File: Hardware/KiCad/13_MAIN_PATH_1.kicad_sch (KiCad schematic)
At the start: 0 parts

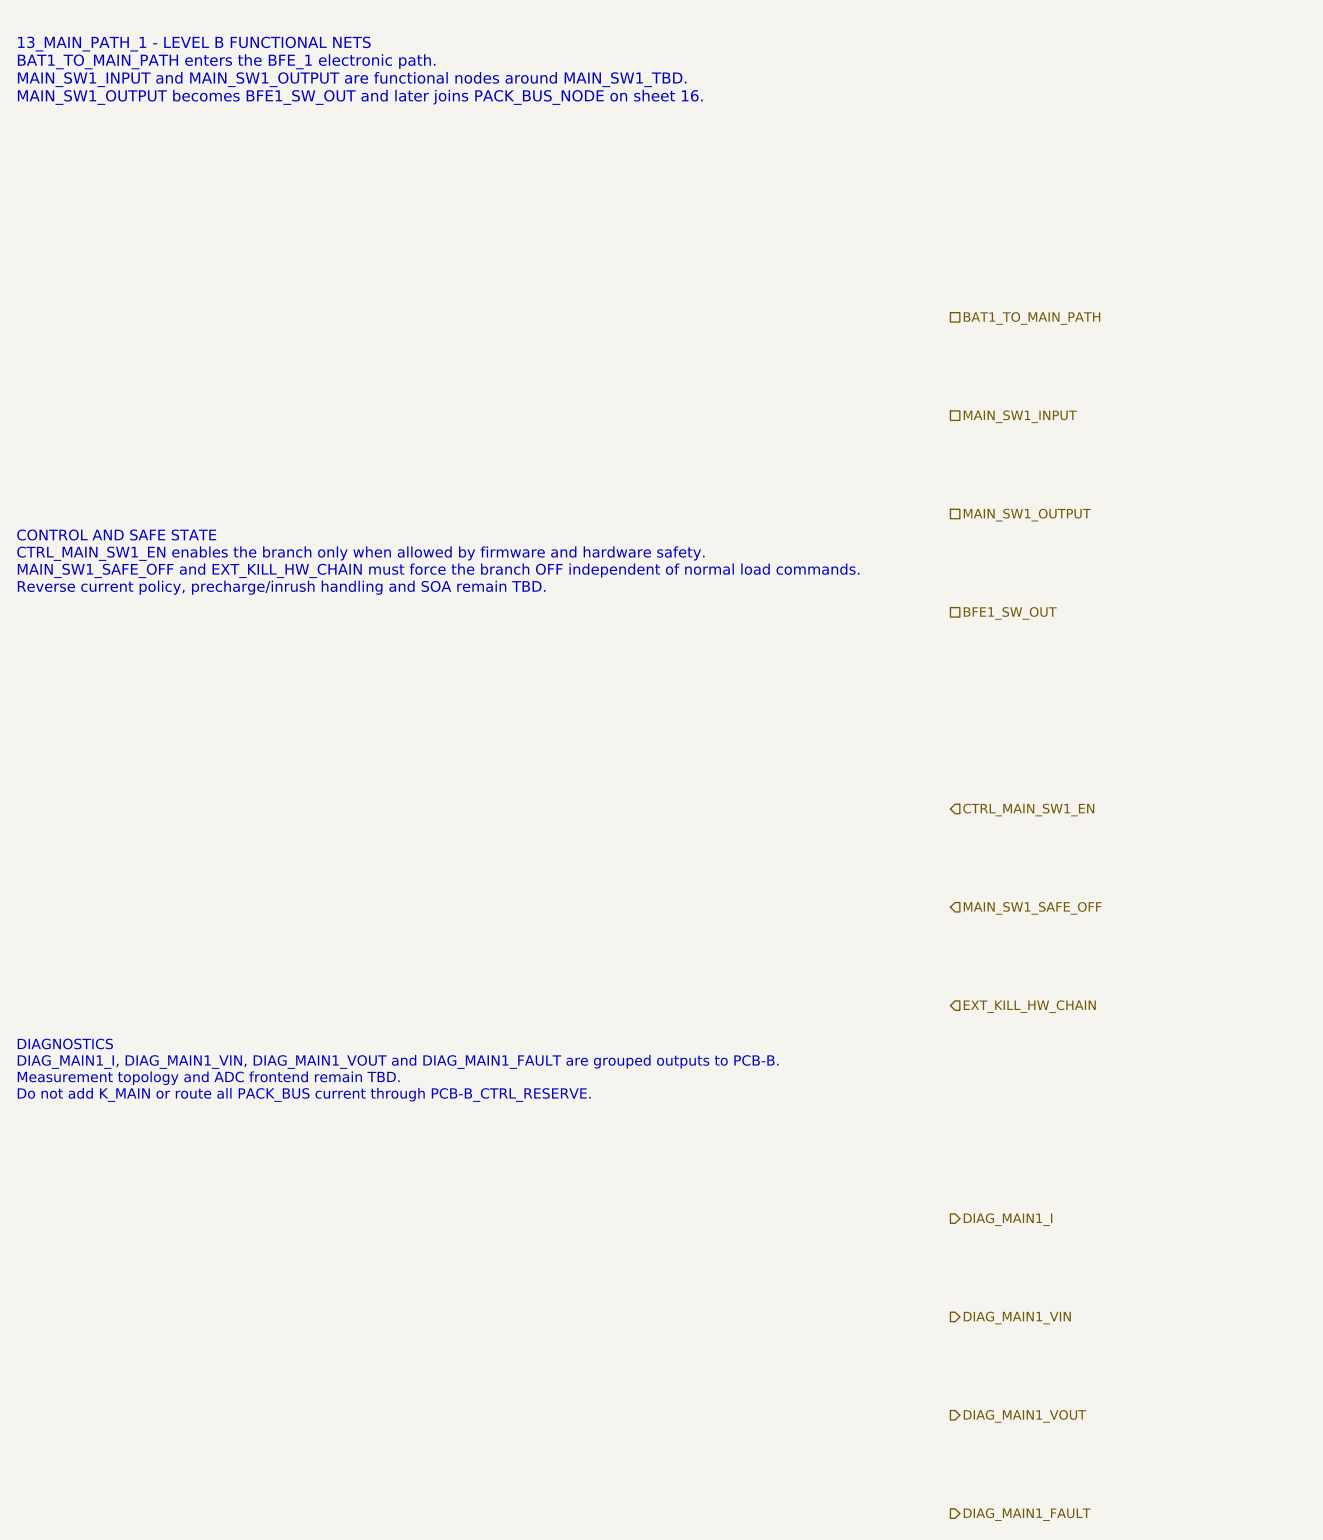
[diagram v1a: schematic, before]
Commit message: hardware: add MAIN_SW1 symbol skeleton zones
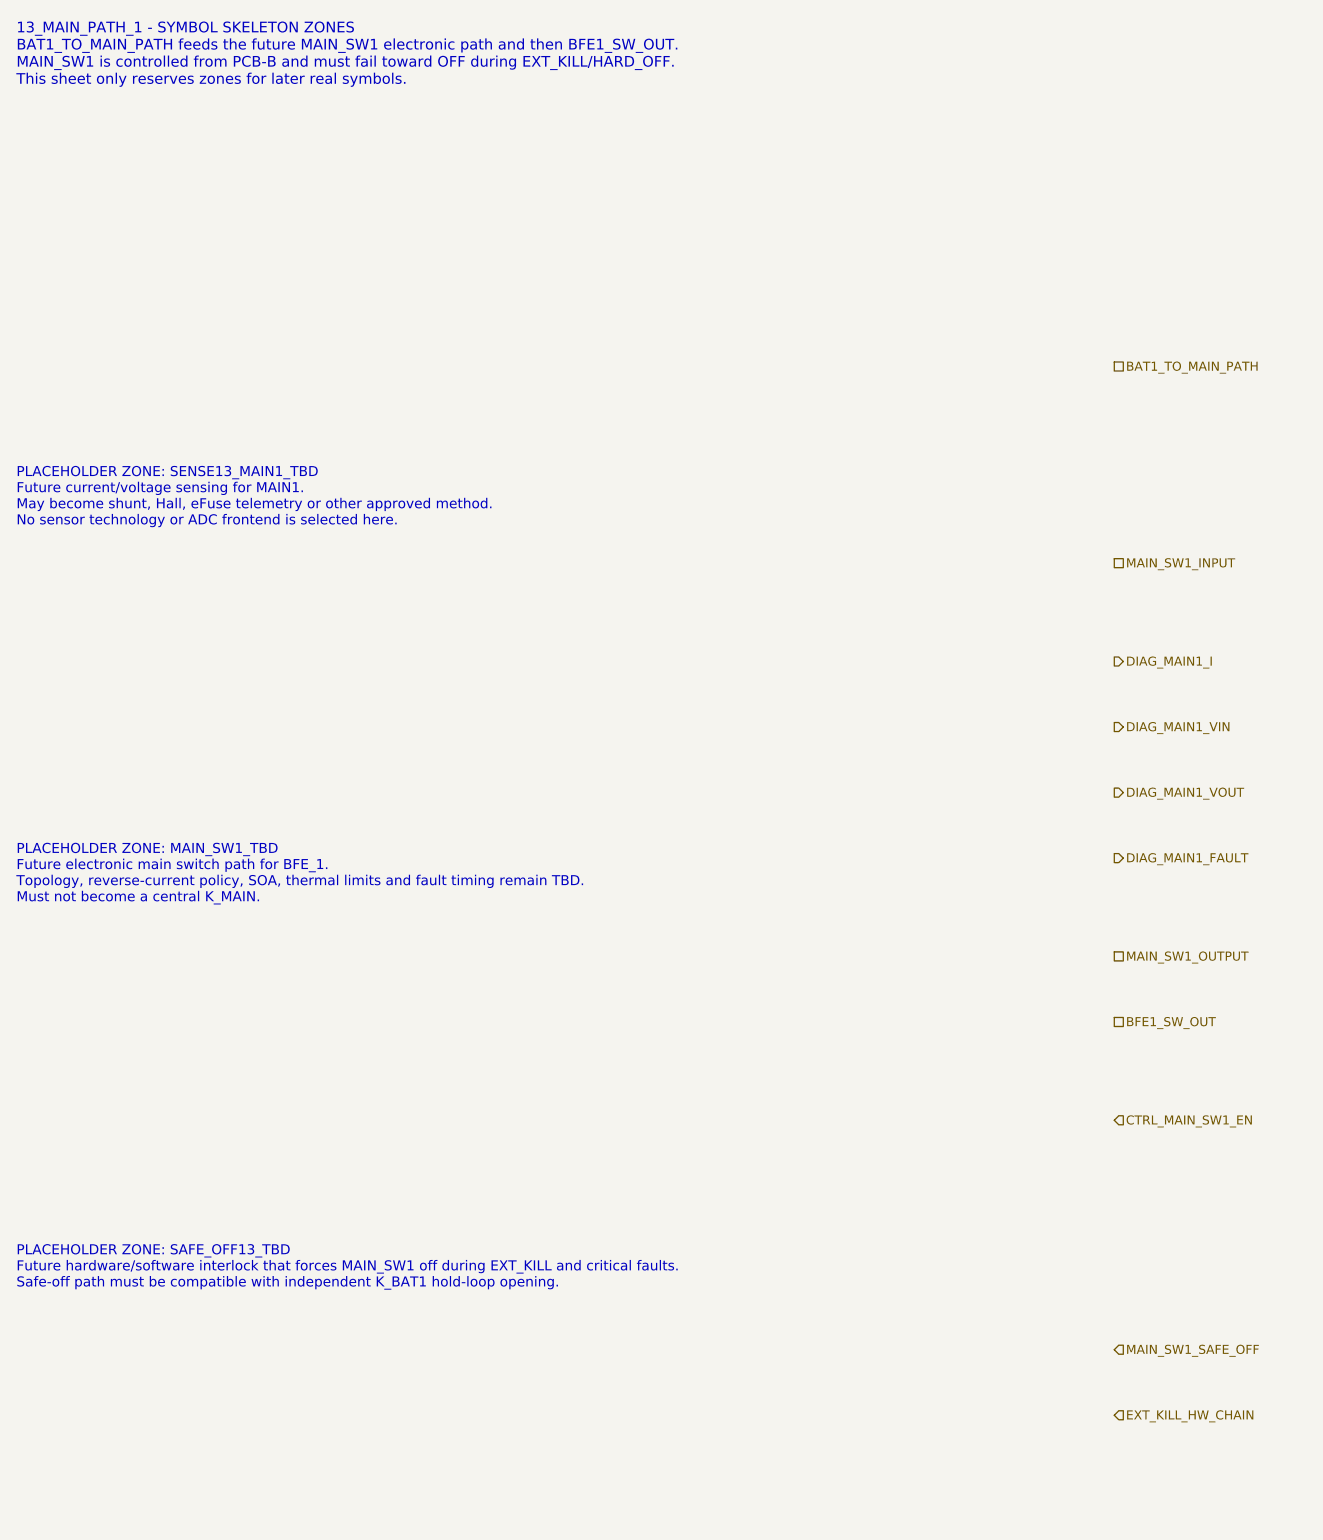
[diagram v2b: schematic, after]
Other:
- note added: "13_MAIN_PATH_1 - SYMBOL SKELETON ZONES BAT1_TO_MAIN_PATH feeds the future MAIN_SW1 electronic path and then BFE1_SW_OUT. MAIN_SW1 is controlled from PCB-B and must fail toward OFF during EXT_KILL/HARD_OFF. This sheet only reserves zones for later real symbols."
- note added: "PLACEHOLDER ZONE: MAIN_SW1_TBD Future electronic main switch path for BFE_1. Topology, reverse-current policy, SOA, thermal limits and fault timing remain TBD. Must not become a central K_MAIN."
- note added: "PLACEHOLDER ZONE: SAFE_OFF13_TBD Future hardware/software interlock that forces MAIN_SW1 off during EXT_KILL and critical faults. Safe-off path must be compatible with independent K_BAT1 hold-loop opening."
- note added: "PLACEHOLDER ZONE: SENSE13_MAIN1_TBD Future current/voltage sensing for MAIN1. May become shunt, Hall, eFuse telemetry or other approved method. No sensor technology or ADC frontend is selected here."
- note removed: "13_MAIN_PATH_1 - LEVEL B FUNCTIONAL NETS BAT1_TO_MAIN_PATH enters the BFE_1 electronic path. MAIN_SW1_INPUT and MAIN_SW1_OUTPUT are functional nodes around MAIN_SW1_TBD. MAIN_SW1_OUTPUT becomes BFE1_SW_OUT and later joins PACK_BUS_NODE on sheet 16."
- note removed: "CONTROL AND SAFE STATE CTRL_MAIN_SW1_EN enables the branch only when allowed by firmware and hardware safety. MAIN_SW1_SAFE_OFF and EXT_KILL_HW_CHAIN must force the branch OFF independent of normal load commands. Reverse current policy, precharge/inrush handling and SOA remain TBD."
- note removed: "DIAGNOSTICS DIAG_MAIN1_I, DIAG_MAIN1_VIN, DIAG_MAIN1_VOUT and DIAG_MAIN1_FAULT are grouped outputs to PCB-B. Measurement topology and ADC frontend remain TBD. Do not add K_MAIN or route all PACK_BUS current through PCB-B_CTRL_RESERVE."
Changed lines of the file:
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@@
 		(title "13_MAIN_PATH_1 - BFE_1 main electronic path")
 		(date "2026-07-15")
-		(rev "B1")
+		(rev "C1")
 		(company "Gonoboben/plataVM")
-		(comment 1 "Architecture Level B: MAIN_SW1 control, diagnostics and safe-state nets")
-		(comment 2 "No MAIN_SW1 topology, MOSFET, eFuse or current sensor selected")
+		(comment 1 "Symbol skeleton: MAIN_SW1, sensing and safe-off placeholders")
+		(comment 2 "No MOSFET, eFuse, ideal-diode, current sensor or footprint selected")
 	)
-	(text "13_MAIN_PATH_1 - LEVEL B FUNCTIONAL NETS\nBAT1_TO_MAIN_PATH enters the BFE_1 electronic path.\nMAIN_SW1_INPUT and MAIN_SW1_OUTPUT are functional nodes around MAIN_SW1_TBD.\nMAIN_SW1_OUTPUT becomes BFE1_SW_OUT and later joins PACK_BUS_NODE on sheet 16."
+	(text "13_MAIN_PATH_1 - SYMBOL SKELETON ZONES\nBAT1_TO_MAIN_PATH feeds the future MAIN_SW1 electronic path and then BFE1_SW_OUT.\nMAIN_SW1 is controlled from PCB-B and must fail toward OFF during EXT_KILL/HARD_OFF.\nThis sheet only reserves zones for later real symbols."
 		(exclude_from_sim no)
-		(at 12 18 0)
-		(effects (font (size 1.35 1.35)) (justify left))
+		(at 12 16 0)
+		(effects (font (size 1.3 1.3)) (justify left))
 		(uuid "bfe-lb-00000013-0000-4000-8000-000000000101")
 	)
-	(text "CONTROL AND SAFE STATE\nCTRL_MAIN_SW1_EN enables the branch only when allowed by firmware and hardware safety.\nMAIN_SW1_SAFE_OFF and EXT_KILL_HW_CHAIN must force the branch OFF independent of normal load commands.\nReverse current policy, precharge/inrush handling and SOA remain TBD."
+	(text "PLACEHOLDER ZONE: SENSE13_MAIN1_TBD\nFuture current/voltage sensing for MAIN1.\nMay become shunt, Hall, eFuse telemetry or other approved method.\nNo sensor technology or ADC frontend is selected here."
 		(exclude_from_sim no)
-		(at 12 78 0)
-		(effects (font (size 1.3 1.3)) (justify left))
+		(at 12 70 0)
+		(effects (font (size 1.22 1.22)) (justify left))
 		(uuid "bfe-lb-00000013-0000-4000-8000-000000000102")
 	)
-	(text "DIAGNOSTICS\nDIAG_MAIN1_I, DIAG_MAIN1_VIN, DIAG_MAIN1_VOUT and DIAG_MAIN1_FAULT are grouped outputs to PCB-B.\nMeasurement topology and ADC frontend remain TBD.\nDo not add K_MAIN or route all PACK_BUS current through PCB-B_CTRL_RESERVE."
+	(text "PLACEHOLDER ZONE: MAIN_SW1_TBD\nFuture electronic main switch path for BFE_1.\nTopology, reverse-current policy, SOA, thermal limits and fault timing remain TBD.\nMust not become a central K_MAIN."
 		(exclude_from_sim no)
-		(at 12 140 0)
-		(effects (font (size 1.25 1.25)) (justify left))
+		(at 12 116 0)
+		(effects (font (size 1.22 1.22)) (justify left))
 		(uuid "bfe-lb-00000013-0000-4000-8000-000000000103")
 	)
-	(hierarchical_label "BAT1_TO_MAIN_PATH" (shape passive) (exclude_from_sim no) (at 126 48 0) (effects (font (size 1.15 1.15)) (justify left)) (uuid "bfe-lb-00000013-0000-4000-8000-000000000201"))
-	(hierarchical_label "MAIN_SW1_INPUT" (shape passive) (exclude_from_sim no) (at 126 60 0) (effects (font (size 1.15 1.15)) (justify left)) (uuid "bfe-lb-00000013-0000-4000-8000-000000000202"))
-	(hierarchical_label "MAIN_SW1_OUTPUT" (shape passive) (exclude_from_sim no) (at 126 72 0) (effects (font (size 1.15 1.15)) (justify left)) (uuid "bfe-lb-00000013-0000-4000-8000-000000000203"))
-	(hierarchical_label "BFE1_SW_OUT" (shape passive) (exclude_from_sim no) (at 126 84 0) (effects (font (size 1.15 1.15)) (justify left)) (uuid "bfe-lb-00000013-0000-4000-8000-000000000204"))
-	(hierarchical_label "CTRL_MAIN_SW1_EN" (shape input) (exclude_from_sim no) (at 126 108 0) (effects (font (size 1.15 1.15)) (justify left)) (uuid "bfe-lb-00000013-0000-4000-8000-000000000205"))
-	(hierarchical_label "MAIN_SW1_SAFE_OFF" (shape input) (exclude_from_sim no) (at 126 120 0) (effects (font (size 1.15 1.15)) (justify left)) (uuid "bfe-lb-00000013-0000-4000-8000-000000000206"))
-	(hierarchical_label "EXT_KILL_HW_CHAIN" (shape input) (exclude_from_sim no) (at 126 132 0) (effects (font (size 1.15 1.15)) (justify left)) (uuid "bfe-lb-00000013-0000-4000-8000-000000000207"))
-	(hierarchical_label "DIAG_MAIN1_I" (shape output) (exclude_from_sim no) (at 126 158 0) (effects (font (size 1.15 1.15)) (justify left)) (uuid "bfe-lb-00000013-0000-4000-8000-000000000208"))
-	(hierarchical_label "DIAG_MAIN1_VIN" (shape output) (exclude_from_sim no) (at 126 170 0) (effects (font (size 1.15 1.15)) (justify left)) (uuid "bfe-lb-00000013-0000-4000-8000-000000000209"))
-	(hierarchical_label "DIAG_MAIN1_VOUT" (shape output) (exclude_from_sim no) (at 126 182 0) (effects (font (size 1.15 1.15)) (justify left)) (uuid "bfe-lb-00000013-0000-4000-8000-000000000210"))
-	(hierarchical_label "DIAG_MAIN1_FAULT" (shape output) (exclude_from_sim no) (at 126 194 0) (effects (font (size 1.15 1.15)) (justify left)) (uuid "bfe-lb-00000013-0000-4000-8000-000000000211"))
+	(text "PLACEHOLDER ZONE: SAFE_OFF13_TBD\nFuture hardware/software interlock that forces MAIN_SW1 off during EXT_KILL and critical faults.\nSafe-off path must be compatible with independent K_BAT1 hold-loop opening."
+		(exclude_from_sim no)
+		(at 12 164 0)
+		(effects (font (size 1.22 1.22)) (justify left))
+		(uuid "bfe-lb-00000013-0000-4000-8000-000000000104")
+	)
+	(hierarchical_label "BAT1_TO_MAIN_PATH" (shape passive) (exclude_from_sim no) (at 146 54 0) (effects (font (size 1.1 1.1)) (justify left)) (uuid "bfe-lb-00000013-0000-4000-8000-000000000201"))
+	(hierarchical_label "MAIN_SW1_INPUT" (shape passive) (exclude_from_sim no) (at 146 78 0) (effects (font (size 1.1 1.1)) (justify left)) (uuid "bfe-lb-00000013-0000-4000-8000-000000000202"))
+	(hierarchical_label "MAIN_SW1_OUTPUT" (shape passive) (exclude_from_sim no) (at 146 126 0) (effects (font (size 1.1 1.1)) (justify left)) (uuid "bfe-lb-00000013-0000-4000-8000-000000000203"))
+	(hierarchical_label "BFE1_SW_OUT" (shape passive) (exclude_from_sim no) (at 146 134 0) (effects (font (size 1.1 1.1)) (justify left)) (uuid "bfe-lb-00000013-0000-4000-8000-000000000204"))
+	(hierarchical_label "CTRL_MAIN_SW1_EN" (shape input) (exclude_from_sim no) (at 146 146 0) (effects (font (size 1.1 1.1)) (justify left)) (uuid "bfe-lb-00000013-0000-4000-8000-000000000205"))
+	(hierarchical_label "MAIN_SW1_SAFE_OFF" (shape input) (exclude_from_sim no) (at 146 174 0) (effects (font (size 1.1 1.1)) (justify left)) (uuid "bfe-lb-00000013-0000-4000-8000-000000000206"))
+	(hierarchical_label "EXT_KILL_HW_CHAIN" (shape input) (exclude_from_sim no) (at 146 182 0) (effects (font (size 1.1 1.1)) (justify left)) (uuid "bfe-lb-00000013-0000-4000-8000-000000000207"))
+	(hierarchical_label "DIAG_MAIN1_I" (shape output) (exclude_from_sim no) (at 146 90 0) (effects (font (size 1.1 1.1)) (justify left)) (uuid "bfe-lb-00000013-0000-4000-8000-000000000208"))
+	(hierarchical_label "DIAG_MAIN1_VIN" (shape output) (exclude_from_sim no) (at 146 98 0) (effects (font (size 1.1 1.1)) (justify left)) (uuid "bfe-lb-00000013-0000-4000-8000-000000000209"))
+	(hierarchical_label "DIAG_MAIN1_VOUT" (shape output) (exclude_from_sim no) (at 146 106 0) (effects (font (size 1.1 1.1)) (justify left)) (uuid "bfe-lb-00000013-0000-4000-8000-000000000210"))
+	(hierarchical_label "DIAG_MAIN1_FAULT" (shape output) (exclude_from_sim no) (at 146 114 0) (effects (font (size 1.1 1.1)) (justify left)) (uuid "bfe-lb-00000013-0000-4000-8000-000000000211"))
 )
